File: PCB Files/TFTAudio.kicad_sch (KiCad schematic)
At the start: 32 parts, among them J1 USB_C_Receptacle_USB2.0_14P, J2 Conn_01x02, J3 Conn_01x14_Socket, J4 Conn_01x06_Socket, J5 Conn_01x12_Pin, Q1 BSS138, Q2 BSS138, Q3 DMG2301L, SW1 SW_SPST, U1 ESP32-WROVER-E, U2 CH340C, U3 MCP73831-2-OT, U4 AP2112K-3.3

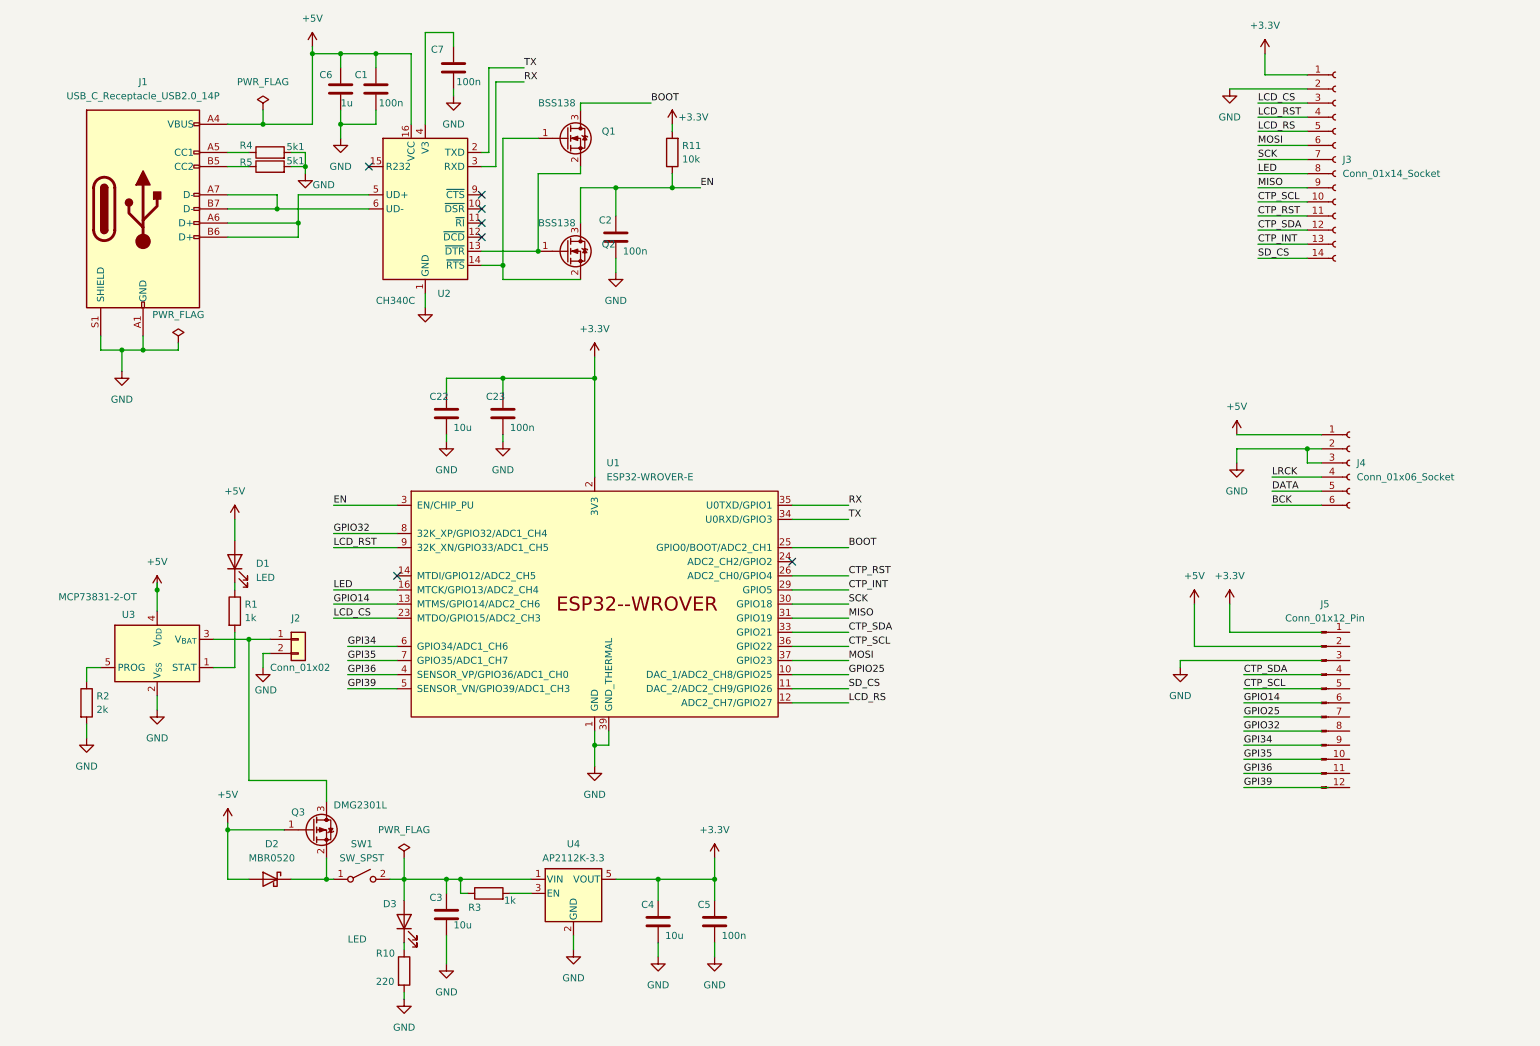
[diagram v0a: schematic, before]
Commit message: added de-coupling to PCB schematic
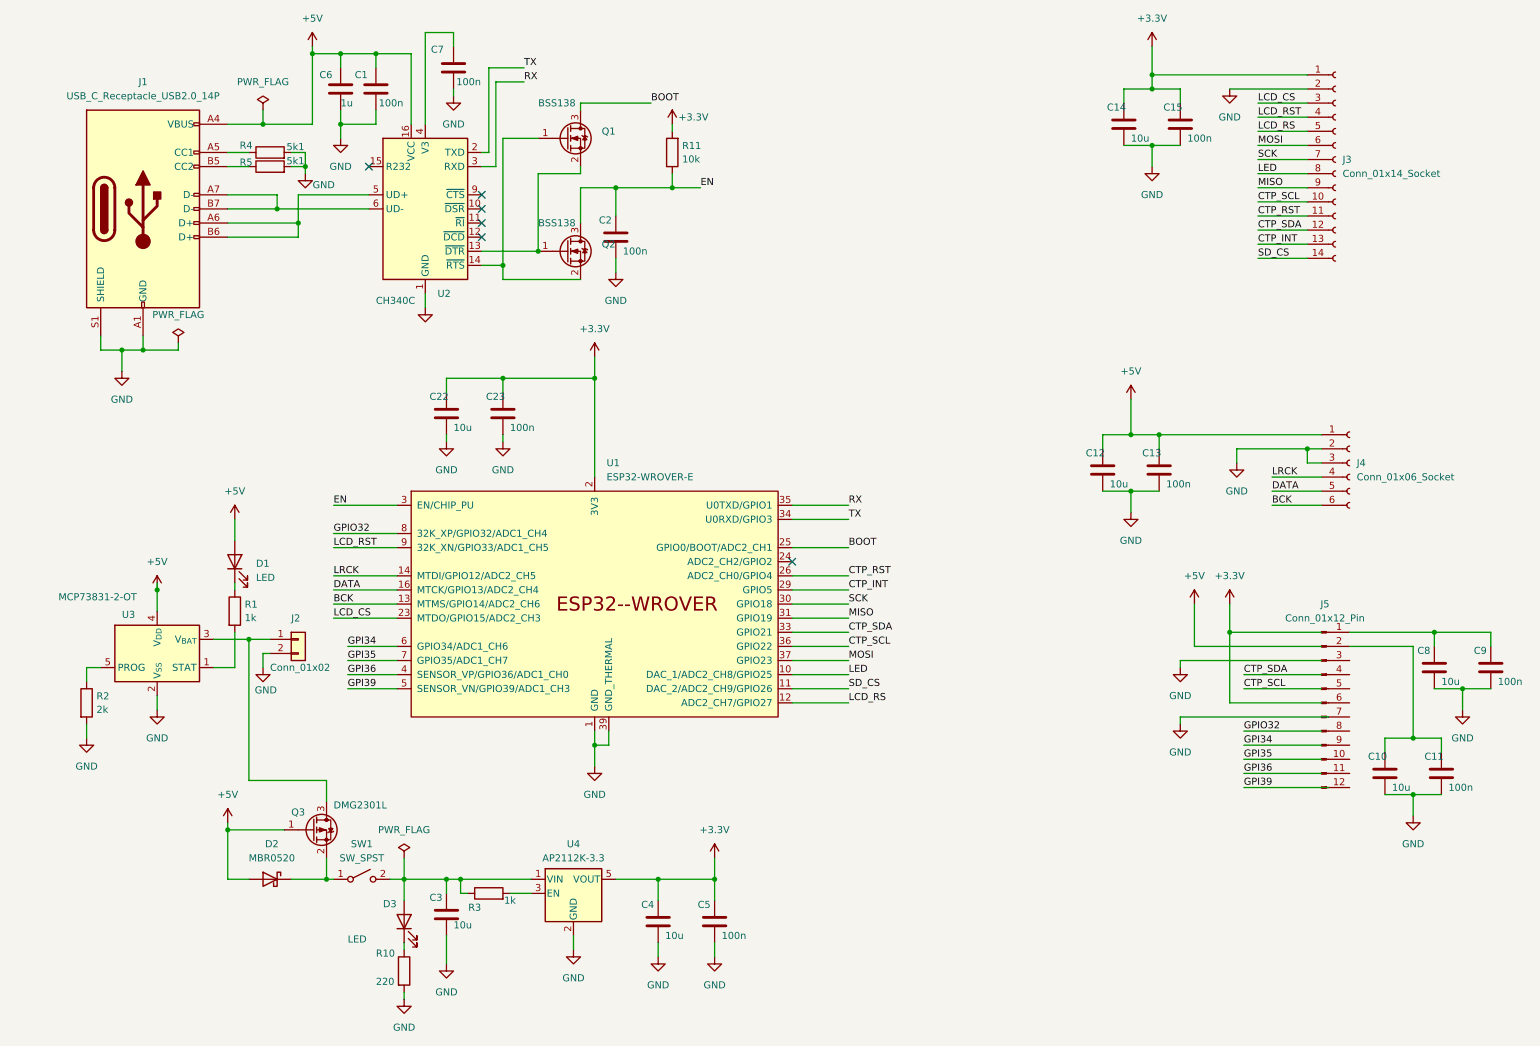
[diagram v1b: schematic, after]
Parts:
- added C10, C12, C14, C8: 10u, Capacitor_SMD:C_0805_2012Metric_Pad1.18x1.45mm_HandSolder, symbol Device:C
- added C11, C13, C15, C9: 100n, Capacitor_SMD:C_0603_1608Metric, symbol Device:C
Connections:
- net GPIO14 is gone; now on net BCK: U1.13 (MTMS/GPIO14/ADC2_CH6)
- net GPIO25 is gone; now on net LED: U1.10 (DAC_1/ADC2_CH8/GPIO25)
- net +3.3V: now also C14.1, C15.1
- net +5V: now also C12.1, C13.1
- net DATA: now also U1.16 (MTCK/GPIO13/ADC2_CH4)
- net GND: now also C10.2, C11.2, C12.2, C13.2, C14.2, C15.2, C8.2, C9.2
- net LED: no longer U1.16 (MTCK/GPIO13/ADC2_CH4)
- net LRCK: now also U1.14 (MTDI/GPIO12/ADC2_CH5)
- net at J5.1 (Pin_1): now also C8.1, C9.1
- net at J5.2 (Pin_2): now also C10.1, C11.1
- no-connect marks 7 -> 6

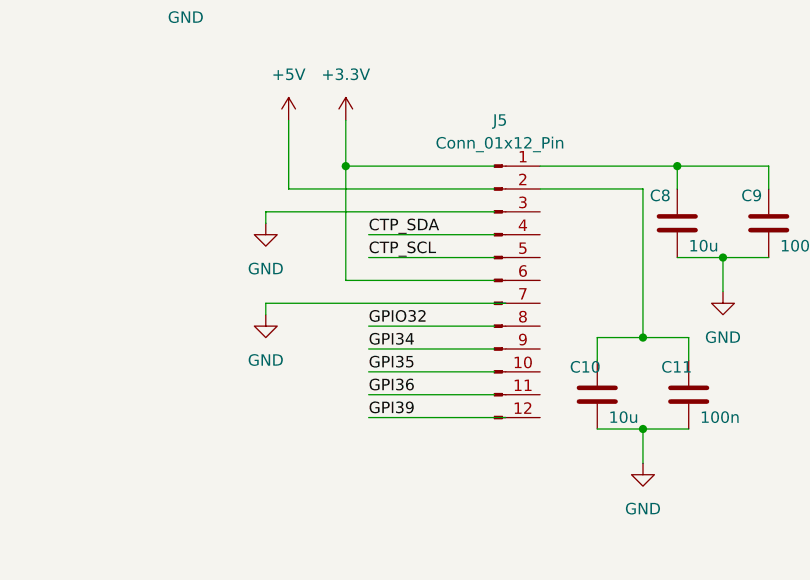
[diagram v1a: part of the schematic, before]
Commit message: minor changes to fix DMA issues.
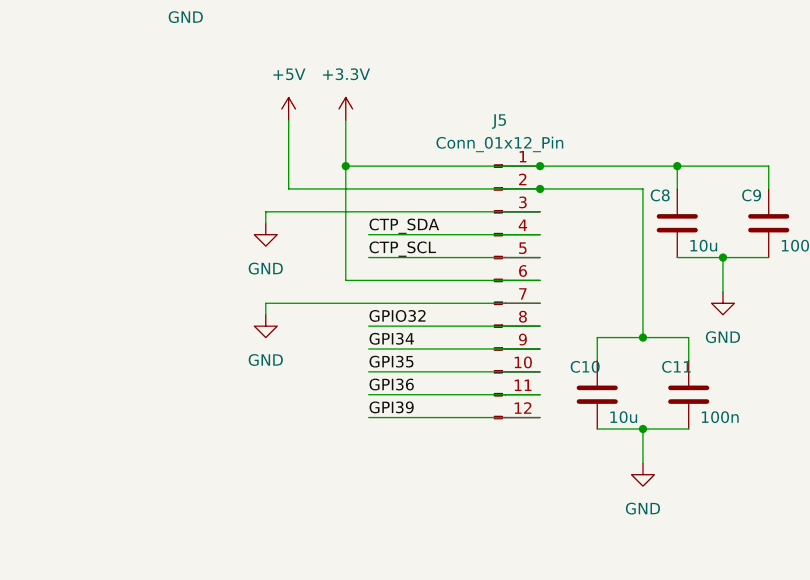
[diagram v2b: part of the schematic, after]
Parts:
- J3: footprint (none) -> Connector_PinSocket_2.54mm:PinSocket_1x14_P2.54mm_Vertical
- J4: footprint (none) -> Connector_PinSocket_2.54mm:PinSocket_1x06_P2.54mm_Vertical
- J5: footprint (none) -> Connector_PinSocket_2.54mm:PinSocket_1x12_P2.54mm_Vertical
- U1: footprint PCM_Espressif:ESP32-WROVER-E -> Espressif:ESP32-WROVER-E
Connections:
- net +3.3V: now also C8.1, C9.1, J5.1 (Pin_1), J5.6 (Pin_6)
- net +5V: now also C10.1, C11.1, J5.2 (Pin_2)
- net CTP_SCL: now also J5.5 (Pin_5)
- net CTP_SDA: now also J5.4 (Pin_4)
- net GND: now also J5.3 (Pin_3), J5.7 (Pin_7)
- net GPI34: now also J5.9 (Pin_9)
- net GPI35: now also J5.10 (Pin_10)
- net GPI36: now also J5.11 (Pin_11)
- net GPI39: now also J5.12 (Pin_12)
- net GPIO32: now also J5.8 (Pin_8)

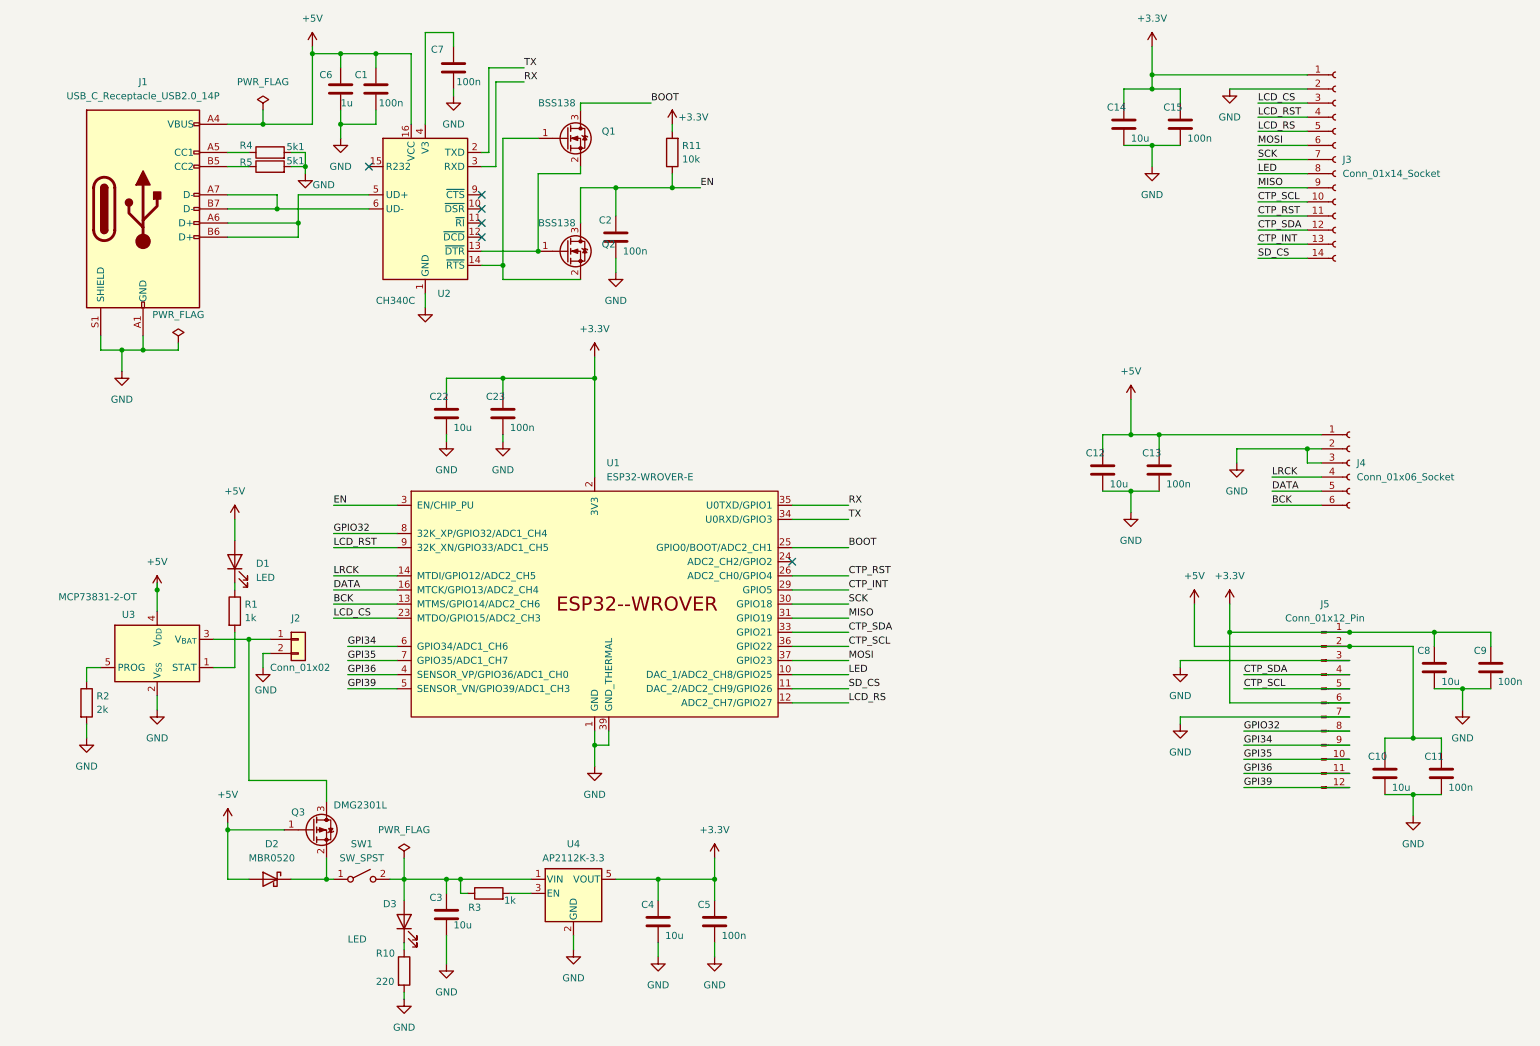
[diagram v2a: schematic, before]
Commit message: uodated PCB files - added PCM5102
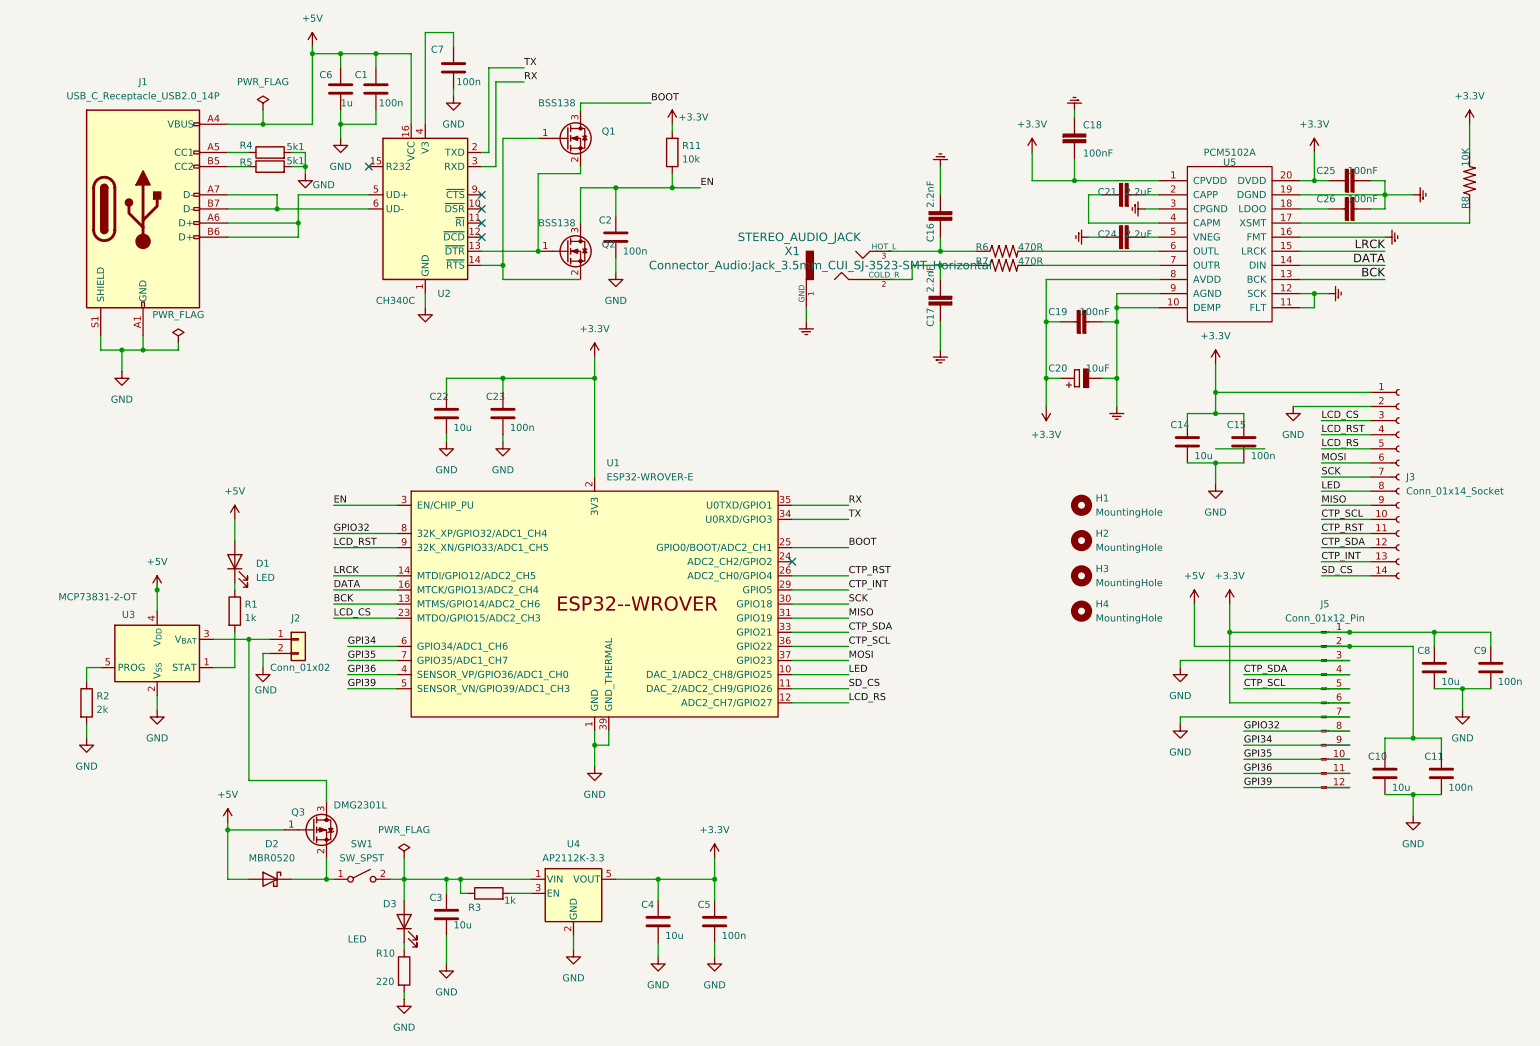
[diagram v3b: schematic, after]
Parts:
- removed C12: 10u, Capacitor_SMD:C_0805_2012Metric_Pad1.18x1.45mm_HandSolder, symbol Device:C
- removed C13: 100n, Capacitor_SMD:C_0603_1608Metric, symbol Device:C
- removed J4: Conn_01x06_Socket, Connector_PinSocket_2.54mm:PinSocket_1x06_P2.54mm_Vertical, symbol Connector:Conn_01x06_Socket
- added C16: 2.2nF, Capacitor_SMD:C_0603_1608Metric, symbol pidac_5102A-rescue:C_EU
- added C17: 2.2nF, Capacitor_SMD:C_0201_0603Metric, symbol pidac_5102A-rescue:C_EU
- added C18, C19, C25, C26: 100nF, Capacitor_SMD:C_0201_0603Metric, symbol pidac_5102A-rescue:C_EU
- added C20: 10uF, Capacitor_SMD:C_0805_2012Metric, symbol pidac_5102A-rescue:CPOL_EU
- added C21: 2.2uF, Capacitor_SMD:C_0805_2012Metric, symbol pidac_5102A-rescue:C_EU
- added C24: 2.2uF, Capacitor_SMD:C_0201_0603Metric, symbol pidac_5102A-rescue:C_EU
- added H1, H2, H3, H4: MountingHole, MountingHole:MountingHole_4.3mm_M4, symbol Mechanical:MountingHole
- added R6, R7: 470R, Resistor_SMD:R_0603_1608Metric, symbol pidac_5102A-rescue:R_US
- added R8: 10K, Resistor_SMD:R_0603_1608Metric, symbol pidac_5102A-rescue:R_US
- added U5: PCM5102A, Package_SO:TSSOP-20_4.4x6.5mm_P0.65mm, symbol pidac_5102A-rescue:PCM5102A
- added X1: STEREO_AUDIO_JACK, Connector_Audio:Jack_3.5mm_CUI_SJ-3523-SMT_Horizontal, symbol pidac_5102A-rescue:STEREO_AUDIO_JACK
- U1: footprint Espressif:ESP32-WROVER-E -> PCM_Espressif:ESP32-WROVER-E
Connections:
- net +3.3V: now also C18.2, C19.1, C20.1 (+), C25.1, R8.2, U5.1 (CPVDD), U5.20 (DVDD), U5.8 (AVDD)
- net BCK: now also U5.13 (BCK)
- net DATA: now also U5.14 (DIN)
- net GND: now also C16.2, C17.1, C18.1, C19.2, C20.2 (-), C24.1, C25.2, C26.2, U5.10 (DEMP), U5.11 (FLT), U5.12 (SCK), U5.16 (FMT), U5.19 (DGND), U5.3 (CPGND), U5.9 (AGND), X1.1 (GND)
- net LRCK: now also U5.15 (LRCK)
- new net: C17.2, R7.1, X1.2 (COLD_R)
- new net: C16.1, R6.1, X1.3 (HOT_L)
- new net: C21.1, U5.4 (CAPM)
- new net: C21.2, U5.2 (CAPP)
- new net: C24.2, U5.5 (VNEG)
- new net: C26.1, U5.18 (LDOO)
- new net: R7.2, U5.7 (OUTR)
- new net: R6.2, U5.6 (OUTL)
- new net: R8.1, U5.17 (XSMT)
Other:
- moved on the sheet: C14, C15, J3

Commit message: Mark R Commit - PCB help
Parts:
- added R9: 100k, Resistor_SMD:R_0603_1608Metric, symbol Device:R
- C10, C14, C22, C3, C4, C8: footprint Capacitor_SMD:C_0805_2012Metric_Pad1.18x1.45mm_HandSolder -> Capacitor_SMD:C_0603_1608Metric
- C17, C18, C19, C24, C25, C26: footprint Capacitor_SMD:C_0201_0603Metric -> Capacitor_SMD:C_0603_1608Metric
- C20, C21: footprint Capacitor_SMD:C_0805_2012Metric -> Capacitor_SMD:C_0603_1608Metric
- D1: value LED -> Charge
- H1, H2, H3, H4: footprint MountingHole:MountingHole_4.3mm_M4 -> MountingHole:MountingHole_3.2mm_M3_ISO14580
- J2: value Conn_01x02 -> Lipo 1S
- J3: value Conn_01x14_Socket -> Display
- J5: value Conn_01x12_Pin -> expansion
- X1: footprint Connector_Audio:Jack_3.5mm_CUI_SJ-3523-SMT_Horizontal -> line out
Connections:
- net +5V: now also R9.1
- net GND: now also R9.2
- net REGIN: now reaches C3.1, D3.2 (A), R3.1, SW1.2 (B), U4.1 (VIN)
- net SWIN: now reaches D2.1 (K), Q3.2 (S), SW1.1 (A)
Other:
- note added: "Charge control"
- moved on the sheet: J5

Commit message: pcb - finished draft 1.0
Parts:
- removed C10: 10u, Capacitor_SMD:C_0603_1608Metric, symbol Device:C
- removed C11: 100n, Capacitor_SMD:C_0603_1608Metric, symbol Device:C
- removed J1: USB_C_Receptacle_USB2.0_14P, Connector_USB:USB_C_Receptacle_JAE_DX07S016JA1R1500, symbol Connector:USB_C_Receptacle_USB2.0_14P
- removed X1: STEREO_AUDIO_JACK, line out, symbol pidac_5102A-rescue:STEREO_AUDIO_JACK
- added J4: AudioJack3, Connector_Audio:Jack_3.5mm_CUI_SJ1-3523N_Horizontal, symbol Connector_Audio:AudioJack3
- added J6: USB_C_Receptacle_USB2.0_14P, Connector_USB:USB_C_Receptacle_HRO_TYPE-C-31-M-12, symbol Connector:USB_C_Receptacle_USB2.0_14P
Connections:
- net +3.3V: now also J5.11 (Pin_11); no longer J5.6 (Pin_6)
- net +5V: now also J6.A4 (VBUS), J6.A9 (VBUS), J6.B4 (VBUS), J6.B9 (VBUS); no longer J5.2 (Pin_2)
- net CTP_INT: now also U1.5 (SENSOR_VN/GPIO39/ADC1_CH3); no longer U1.29 (GPIO5)
- net CTP_RST: now also U1.11 (DAC_2/ADC2_CH9/GPIO26); no longer U1.26 (ADC2_CH0/GPIO4)
- net CTP_SCL: now also J5.4 (Pin_4); no longer J5.5 (Pin_5)
- net CTP_SDA: now also J5.3 (Pin_3); no longer J5.4 (Pin_4)
- net GND: now also J5.12 (Pin_12), J5.2 (Pin_2), J4.S, J6.A1 (GND), J6.A12 (GND), J6.B1 (GND), J6.B12 (GND), J6.S1 (SHIELD); no longer J5.3 (Pin_3), J5.7 (Pin_7)
- net GPI35: now also J5.9 (Pin_9); no longer J5.10 (Pin_10)
- net GPI36: now also J5.10 (Pin_10); no longer J5.11 (Pin_11)
- net LCD_CS: now also U1.9 (32K_XN/GPIO33/ADC1_CH5); no longer U1.23 (MTDO/GPIO15/ADC2_CH3)
- net LCD_RST: now also U1.8 (32K_XP/GPIO32/ADC1_CH4); no longer U1.9 (32K_XN/GPIO33/ADC1_CH5)
- net MISO: now also U1.6 (GPIO34/ADC1_CH6); no longer U1.31 (GPIO19)
- net SD_CS: now also J5.5 (Pin_5), U1.29 (GPIO5); no longer U1.11 (DAC_2/ADC2_CH9/GPIO26)
- net at C17.2, R7.1: now also J4.R
- net at C16.1, R6.1: now also J4.T
- net at U2.5 (UD+): now also J6.A6 (D+), J6.B6 (D+)
- net at U2.6 (UD-): now also J6.A7 (D-), J6.B7 (D-)
- net at R4.1: now also J6.A5 (CC1)
- net at R5.1: now also J6.B5 (CC2)
- removed net GPI34: J5.9 (Pin_9), U1.6 (GPIO34/ADC1_CH6)
- removed net GPI39: J5.12 (Pin_12), U1.5 (SENSOR_VN/GPIO39/ADC1_CH3)
- net GPIO32 renamed GPIO19
- net GPIO19: now also U1.31 (GPIO19); no longer U1.8 (32K_XP/GPIO32/ADC1_CH4)
- new net GPIO15: J5.7 (Pin_7), U1.23 (MTDO/GPIO15/ADC2_CH3)
- new net GPIO4: J5.6 (Pin_6), U1.26 (ADC2_CH0/GPIO4)
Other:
- moved on the sheet: C8, C9
